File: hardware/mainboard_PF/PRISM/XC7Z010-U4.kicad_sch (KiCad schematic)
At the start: 1 part, among them U1 XC7Z010-1CLG400C

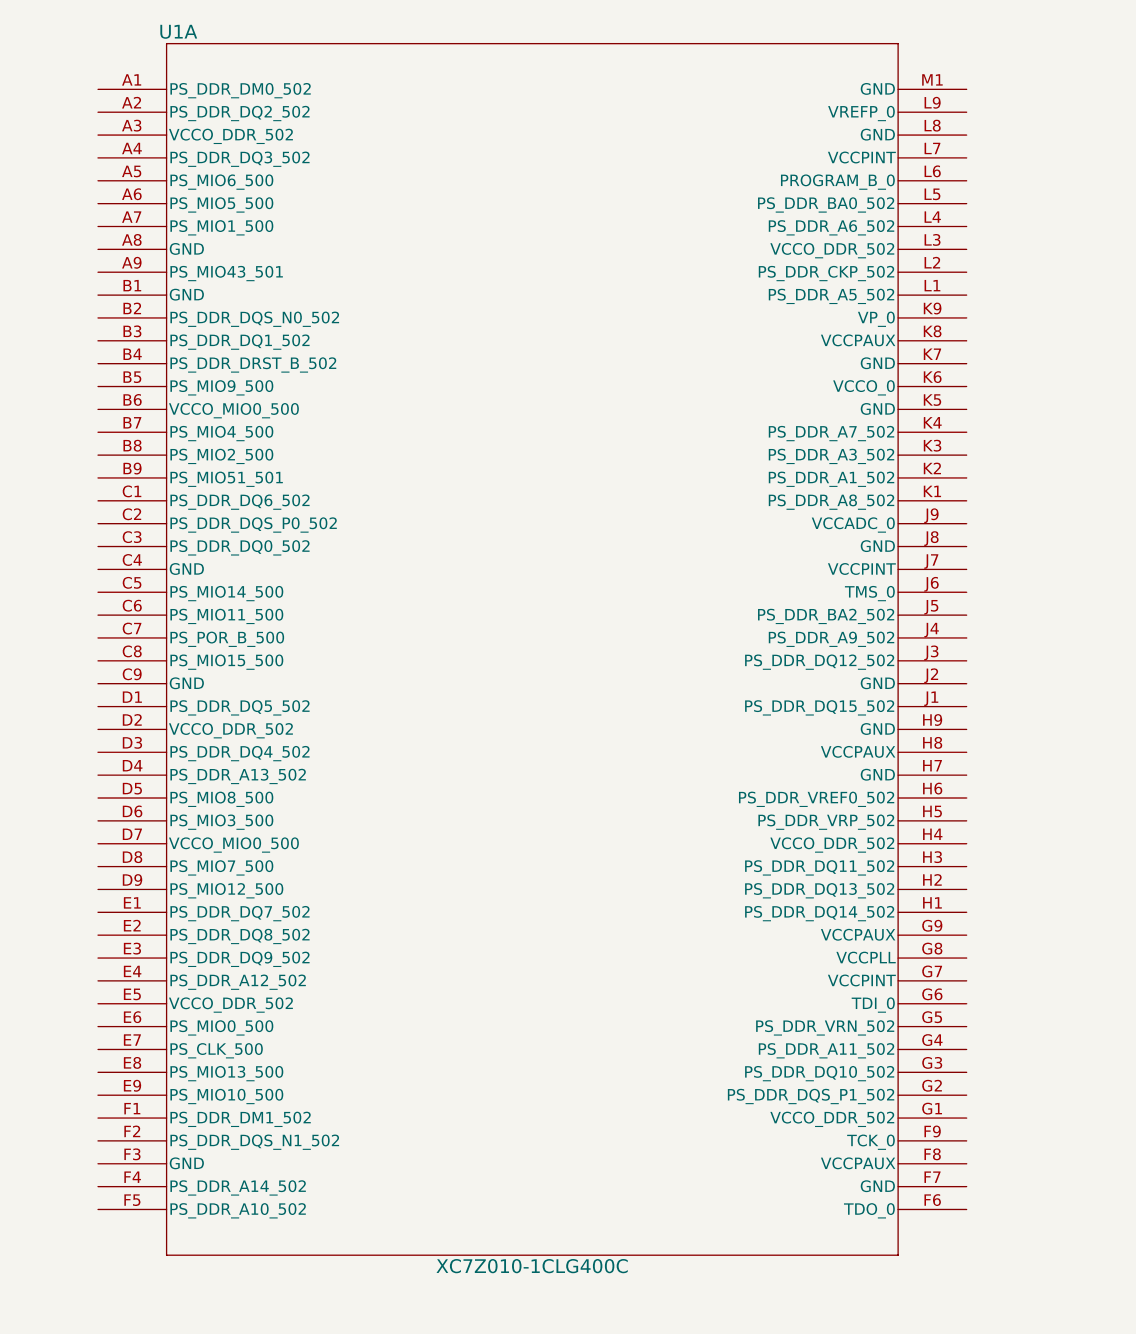
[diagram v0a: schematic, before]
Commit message: More Protoflow
Power Systesm
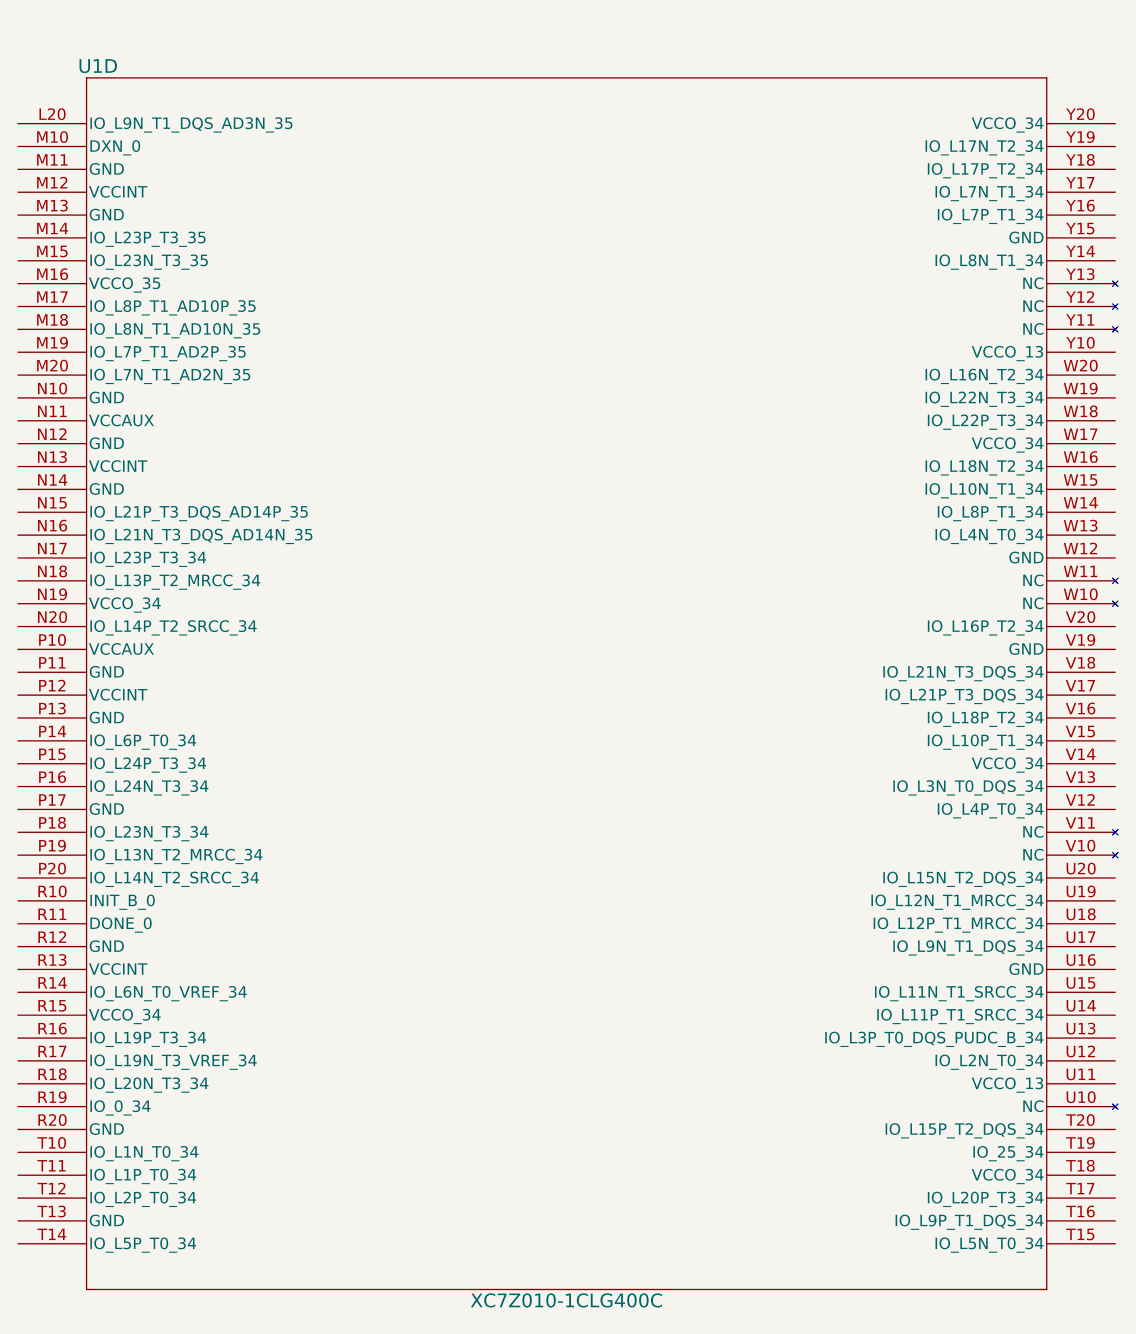
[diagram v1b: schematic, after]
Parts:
- removed U1: XC7Z010-1CLG400C, ProtoFlow.pretty:CLG400_XIL, symbol XC7Z010-1CLG400C
- added U1: XC7Z010-1CLG400C, ProtoFlow.pretty:CLG400_XIL, symbol XC7Z010-1CLG400C
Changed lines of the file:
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@@
     (company "Protoflow")
   )
-  (symbol (lib_id "XC7Z010-1CLG400C") (at 100.33 35.56 0)
-    (unit 1)
+  (symbol (lib_id "XC7Z010-1CLG400C") (at 91.44 39.37 0)
+    (unit 4)
     (convert 1)
     (in_bom yes)
     (on_board yes)
-    (property "Reference" "U1" (id 0) (at 109.22 29.21 0) (effects (font (size 1.524 1.524))))
-    (property "Value" "XC7Z010-1CLG400C" (id 1) (at 148.59 166.37 0) (effects (font (size 1.524 1.524))))
-    (property "Footprint" "ProtoFlow.pretty:CLG400_XIL" (id 2) (at 100.33 35.56 0) (effects (font (size 1.27 1.27)) hide))
-    (property "Datasheet" "XC7Z010-1CLG400C" (id 3) (at 100.33 35.56 0) (effects (font (size 1.27 1.27)) hide))
-    (property "Protoflow_Source" "kicad" (id 4) (at 100.33 35.56 0) (effects (font (size 1.27 1.27)) hide))
-    (pin "A1")
-    (pin "A2")
-    (pin "A3")
-    (pin "A4")
-    (pin "A5")
-    (pin "A6")
-    (pin "A7")
-    (pin "A8")
-    (pin "A9")
-    (pin "B1")
-    (pin "B2")
-    (pin "B3")
-    (pin "B4")
-    (pin "B5")
-    (pin "B6")
-    (pin "B7")
-    (pin "B8")
-    (pin "B9")
-    (pin "C1")
-    (pin "C2")
-    (pin "C3")
-    (pin "C4")
-    (pin "C5")
-    (pin "C6")
-    (pin "C7")
-    (pin "C8")
-    (pin "C9")
-    (pin "D1")
-    (pin "D2")
-    (pin "D3")
-    (pin "D4")
-    (pin "D5")
-    (pin "D6")
-    (pin "D7")
-    (pin "D8")
-    (pin "D9")
-    (pin "E1")
-    (pin "E2")
-    (pin "E3")
-    (pin "E4")
-    (pin "E5")
-    (pin "E6")
-    (pin "E7")
-    (pin "E8")
-    (pin "E9")
-    (pin "F1")
-    (pin "F2")
-    (pin "F3")
-    (pin "F4")
-    (pin "F5")
-    (pin "F6")
-    (pin "F7")
-    (pin "F8")
-    (pin "F9")
-    (pin "G1")
-    (pin "G2")
-    (pin "G3")
-    (pin "G4")
-    (pin "G5")
-    (pin "G6")
-    (pin "G7")
-    (pin "G8")
-    (pin "G9")
-    (pin "H1")
-    (pin "H2")
-    (pin "H3")
-    (pin "H4")
-    (pin "H5")
-    (pin "H6")
-    (pin "H7")
-    (pin "H8")
-    (pin "H9")
-    (pin "J1")
-    (pin "J2")
-    (pin "J3")
-    (pin "J4")
-    (pin "J5")
-    (pin "J6")
-    (pin "J7")
-    (pin "J8")
-    (pin "J9")
-    (pin "K1")
-    (pin "K2")
-    (pin "K3")
-    (pin "K4")
-    (pin "K5")
-    (pin "K6")
-    (pin "K7")
-    (pin "K8")
-    (pin "K9")
-    (pin "L1")
-    (pin "L2")
-    (pin "L3")
-    (pin "L4")
-    (pin "L5")
-    (pin "L6")
-    (pin "L7")
-    (pin "L8")
-    (pin "L9")
-    (pin "M1")
+    (property "Reference" "U1" (id 0) (at 100.33 33.02 0) (effects (font (size 1.524 1.524))))
+    (property "Value" "XC7Z010-1CLG400C" (id 1) (at 152.4 170.18 0) (effects (font (size 1.524 1.524))))
+    (property "Footprint" "ProtoFlow.pretty:CLG400_XIL" (id 2) (at 91.44 39.37 0) (effects (font (size 1.27 1.27)) hide))
+    (property "Datasheet" "XC7Z010-1CLG400C" (id 3) (at 91.44 39.37 0) (effects (font (size 1.27 1.27)) hide))
+    (property "Protoflow_Source" "kicad" (id 4) (at 91.44 39.37 0) (effects (font (size 1.27 1.27)) hide))
+    (pin "L20")
+    (pin "M10")
+    (pin "M11")
+    (pin "M12")
+    (pin "M13")
+    (pin "M14")
+    (pin "M15")
+    (pin "M16")
+    (pin "M17")
+    (pin "M18")
+    (pin "M19")
+    (pin "M20")
+    (pin "N10")
+    (pin "N11")
+    (pin "N12")
+    (pin "N13")
+    (pin "N14")
+    (pin "N15")
+    (pin "N16")
+    (pin "N17")
+    (pin "N18")
+    (pin "N19")
+    (pin "N20")
+    (pin "P10")
+    (pin "P11")
+    (pin "P12")
+    (pin "P13")
+    (pin "P14")
+    (pin "P15")
+    (pin "P16")
+    (pin "P17")
+    (pin "P18")
+    (pin "P19")
+    (pin "P20")
+    (pin "R10")
+    (pin "R11")
+    (pin "R12")
+    (pin "R13")
+    (pin "R14")
+    (pin "R15")
+    (pin "R16")
+    (pin "R17")
+    (pin "R18")
+    (pin "R19")
+    (pin "R20")
+    (pin "T10")
+    (pin "T11")
+    (pin "T12")
+    (pin "T13")
+    (pin "T14")
+    (pin "T15")
+    (pin "T16")
+    (pin "T17")
+    (pin "T18")
+    (pin "T19")
+    (pin "T20")
+    (pin "U10")
+    (pin "U11")
+    (pin "U12")
+    (pin "U13")
+    (pin "U14")
+    (pin "U15")
+    (pin "U16")
+    (pin "U17")
+    (pin "U18")
+    (pin "U19")
+    (pin "U20")
+    (pin "V10")
+    (pin "V11")
+    (pin "V12")
+    (pin "V13")
+    (pin "V14")
+    (pin "V15")
+    (pin "V16")
+    (pin "V17")
+    (pin "V18")
+    (pin "V19")
+    (pin "V20")
+    (pin "W10")
+    (pin "W11")
+    (pin "W12")
+    (pin "W13")
+    (pin "W14")
+    (pin "W15")
+    (pin "W16")
+    (pin "W17")
+    (pin "W18")
+    (pin "W19")
+    (pin "W20")
+    (pin "Y10")
+    (pin "Y11")
+    (pin "Y12")
+    (pin "Y13")
+    (pin "Y14")
+    (pin "Y15")
+    (pin "Y16")
+    (pin "Y17")
+    (pin "Y18")
+    (pin "Y19")
+    (pin "Y20")
     (instances
       (project "protoflow"
-        (path "/" (reference "U1") (unit 1))
+        (path "/" (reference "U1") (unit 4))
       )
     )
